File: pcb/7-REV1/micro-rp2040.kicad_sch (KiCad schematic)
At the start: 60 parts, among them J201 Conn_01x03, J202 TYPE-C-31-M-12, Q1 MMBT7002K, Q2 MMBT7002K, SW101 TS3425BA 098 2.5H 250gf, SW102 TS3315A 250gf 025, U1 RP2350B, U102 W25Q128JVSIQ, U105 MT29F1G01ABAFDWB, U16 SP3002-04JTG, U3 TLV74311PDBVR, U401 ME6211A33PG-N, U8 APS6404L-3SQR-ZR, Y101 ABM8-272-T3

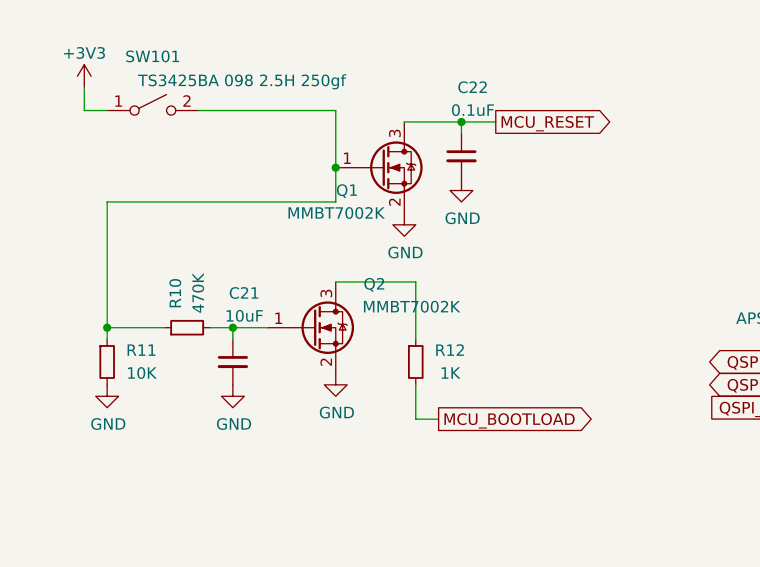
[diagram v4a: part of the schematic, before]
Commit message: replace MMBT7002K in SOT-23 with 2N7002T in SOT-523
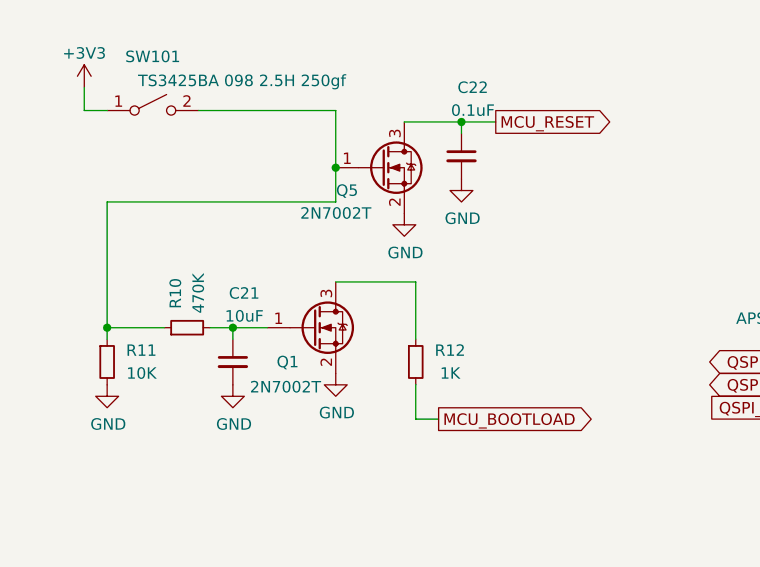
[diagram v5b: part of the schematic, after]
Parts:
- removed Q2: MMBT7002K, Package_TO_SOT_SMD:SOT-23, symbol Transistor_FET:BSS138
- added Q5: 2N7002T, Package_TO_SOT_SMD:SOT-523, symbol Transistor_FET:BSS138
- Q1: value MMBT7002K -> 2N7002T; footprint Package_TO_SOT_SMD:SOT-23 -> Package_TO_SOT_SMD:SOT-523
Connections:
- net GND: now also Q5.2 (S)
- net MCU_RESET: now also Q5.3 (D); no longer Q1.3 (D)
- net at R10.1, R11.1, SW101.2 (B): now also Q5.1 (G); no longer Q1.1 (G)
- net at C21.1, R10.2: now also Q1.1 (G)
- net at R12.1: now also Q1.3 (D)
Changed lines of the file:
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@@
 	)
 	(junction
-		(at 54.61 127)
-		(diameter 0)
-		(color 0 0 0 0)
-	)
-	(junction
 		(at 114.3 36.83)
 		(diameter 0)
@@
 		(color 0 0 0 0)
 	)
+	(junction
+		(at 54.61 127)
+		(diameter 0)
+		(color 0 0 0 0)
+	)
 	(no_connect
 		(at 90.17 41.91)
@@
 	(wire
 		(pts
-			(xy 54.61 130.81) (xy 54.61 127)
-		)
-		(stroke
-			(width 0)
-			(type default)
-		)
-	)
-	(wire
-		(pts
 			(xy 228.6 146.05) (xy 219.71 146.05)
 		)
@@
 	(wire
 		(pts
+			(xy 54.61 127) (xy 54.61 130.81)
+		)
+		(stroke
+			(width 0)
+			(type default)
+		)
+	)
+	(wire
+		(pts
 			(xy 325.12 41.91) (xy 327.66 41.91)
 		)
@@
 	)
 	(symbol
-		(lib_id "Transistor_FET:BSS138")
-		(at 52.07 144.78 0)
-		(unit 1)
-		(exclude_from_sim no)
-		(in_bom yes)
-		(on_board yes)
-		(dnp no)
-		(property "Reference" "Q2"
-			(at 58.928 139.954 0)
-			(effects
-				(font
-					(size 1.27 1.27)
-				)
-			)
-		)
-		(property "Value" "MMBT7002K"
-			(at 62.992 142.494 0)
-			(effects
-				(font
-					(size 1.27 1.27)
-				)
-			)
-		)
-		(property "Footprint" "Package_TO_SOT_SMD:SOT-23"
-			(at 57.15 146.685 0)
-			(effects
-				(font
-					(size 1.27 1.27)
-					(italic yes)
-				)
-				(justify left)
-				(hide yes)
-			)
-		)
-		(property "Datasheet" "https://www.fairchildsemi.com/datasheets/BS/BSS138.pdf"
-			(at 52.07 144.78 0)
-			(effects
-				(font
-					(size 1.27 1.27)
-				)
-				(justify left)
-				(hide yes)
-			)
-		)
-		(property "Description" ""
-			(at 52.07 144.78 0)
-			(effects
-				(font
-					(size 1.27 1.27)
-				)
-				(hide yes)
-			)
-		)
-		(property "RMB" "0.140017"
-			(at 52.07 144.78 0)
-			(effects
-				(font
-					(size 1.27 1.27)
-				)
-				(hide yes)
-			)
-		)
-		(property "Supplier" "https://item.szlcsc.com/544697.html"
-			(at 52.07 144.78 0)
-			(effects
-				(font
-					(size 1.27 1.27)
-				)
-				(hide yes)
-			)
-		)
-		(pin "1"
-		)
-		(pin "2"
-		)
-		(pin "3"
-		)
-		(instances
-			(project "7-REV0"
-				(path "/1f56410a-eaac-4444-b0f7-cfd3531e22ac/00000000-0000-0000-0000-000060c8ec36"
-					(reference "Q2")
-					(unit 1)
-				)
-			)
-		)
-	)
-	(symbol
 		(lib_id "power:GND")
 		(at 120.65 163.83 0)
@@
 	)
 	(symbol
+		(lib_id "Transistor_FET:BSS138")
+		(at 59.69 127 0)
+		(unit 1)
+		(exclude_from_sim no)
+		(in_bom yes)
+		(on_board yes)
+		(dnp no)
+		(property "Reference" "Q5"
+			(at 55.88 129.54 0)
+			(effects
+				(font
+					(size 1.27 1.27)
+				)
+			)
+		)
+		(property "Value" "2N7002T"
+			(at 54.61 132.08 0)
+			(effects
+				(font
+					(size 1.27 1.27)
+				)
+			)
+		)
+		(property "Footprint" "Package_TO_SOT_SMD:SOT-523"
+			(at 64.77 128.905 0)
+			(effects
+				(font
+					(size 1.27 1.27)
+					(italic yes)
+				)
+				(justify left)
+				(hide yes)
+			)
+		)
+		(property "Datasheet" "https://www.onsemi.com/download/data-sheet/pdf/2n7002t-d.pdf"
+			(at 59.69 127 0)
+			(effects
+				(font
+					(size 1.27 1.27)
+				)
+				(justify left)
+				(hide yes)
+			)
+		)
+		(property "Description" ""
+			(at 59.69 127 0)
+			(effects
+				(font
+					(size 1.27 1.27)
+				)
+				(hide yes)
+			)
+		)
+		(property "RMB" "0.140017"
+			(at 59.69 127 0)
+			(effects
+				(font
+					(size 1.27 1.27)
+				)
+				(hide yes)
+			)
+		)
+		(property "Supplier" "https://item.szlcsc.com/544697.html"
+			(at 59.69 127 0)
+			(effects
+				(font
+					(size 1.27 1.27)
+				)
+				(hide yes)
+			)
+		)
+		(pin "1"
+		)
+		(pin "2"
+		)
+		(pin "3"
+		)
+		(instances
+			(project "7-REV1"
+				(path "/1f56410a-eaac-4444-b0f7-cfd3531e22ac/00000000-0000-0000-0000-000060c8ec36"
+					(reference "Q5")
+					(unit 1)
+				)
+			)
+		)
+	)
+	(symbol
 		(lib_id "dp-memory:xm25qh128a")
 		(at 120.65 158.75 0)
@@
 	)
 	(symbol
-		(lib_id "Transistor_FET:BSS138")
-		(at 59.69 127 0)
-		(unit 1)
-		(exclude_from_sim no)
-		(in_bom yes)
-		(on_board yes)
-		(dnp no)
-		(property "Reference" "Q1"
-			(at 55.88 129.54 0)
-			(effects
-				(font
-					(size 1.27 1.27)
-				)
-			)
-		)
-		(property "Value" "MMBT7002K"
-			(at 54.61 132.08 0)
-			(effects
-				(font
-					(size 1.27 1.27)
-				)
-			)
-		)
-		(property "Footprint" "Package_TO_SOT_SMD:SOT-23"
-			(at 64.77 128.905 0)
-			(effects
-				(font
-					(size 1.27 1.27)
-					(italic yes)
-				)
-				(justify left)
-				(hide yes)
-			)
-		)
-		(property "Datasheet" "https://www.fairchildsemi.com/datasheets/BS/BSS138.pdf"
-			(at 59.69 127 0)
-			(effects
-				(font
-					(size 1.27 1.27)
-				)
-				(justify left)
-				(hide yes)
-			)
-		)
-		(property "Description" ""
-			(at 59.69 127 0)
-			(effects
-				(font
-					(size 1.27 1.27)
-				)
-				(hide yes)
-			)
-		)
-		(property "RMB" "0.140017"
-			(at 59.69 127 0)
-			(effects
-				(font
-					(size 1.27 1.27)
-				)
-				(hide yes)
-			)
-		)
-		(property "Supplier" "https://item.szlcsc.com/544697.html"
-			(at 59.69 127 0)
-			(effects
-				(font
-					(size 1.27 1.27)
-				)
-				(hide yes)
-			)
-		)
-		(pin "1"
-		)
-		(pin "2"
-		)
-		(pin "3"
-		)
-		(instances
-			(project "7-REV0"
-				(path "/1f56410a-eaac-4444-b0f7-cfd3531e22ac/00000000-0000-0000-0000-000060c8ec36"
-					(reference "Q1")
-					(unit 1)
-				)
-			)
-		)
-	)
-	(symbol
 		(lib_id "power:GND")
 		(at 43.18 151.13 0)
@@
 					(unit 1)
 				)
+			)
+		)
+	)
+	(symbol
+		(lib_id "Transistor_FET:BSS138")
+		(at 52.07 144.78 0)
+		(unit 1)
+		(exclude_from_sim no)
+		(in_bom yes)
+		(on_board yes)
+		(dnp no)
+		(property "Reference" "Q1"
+			(at 49.276 148.59 0)
+			(effects
+				(font
+					(size 1.27 1.27)
+				)
+			)
+		)
+		(property "Value" "2N7002T"
+			(at 49.022 151.384 0)
+			(effects
+				(font
+					(size 1.27 1.27)
+				)
+			)
+		)
+		(property "Footprint" "Package_TO_SOT_SMD:SOT-523"
+			(at 57.15 146.685 0)
+			(effects
+				(font
+					(size 1.27 1.27)
+					(italic yes)
+				)
+				(justify left)
+				(hide yes)
+			)
+		)
+		(property "Datasheet" "https://www.onsemi.com/download/data-sheet/pdf/2n7002t-d.pdf"
+			(at 52.07 144.78 0)
+			(effects
+				(font
+					(size 1.27 1.27)
+				)
+				(justify left)
+				(hide yes)
+			)
+		)
+		(property "Description" ""
+			(at 52.07 144.78 0)
+			(effects
+				(font
+					(size 1.27 1.27)
+				)
+				(hide yes)
+			)
+		)
+		(property "RMB" "0.140017"
+			(at 52.07 144.78 0)
+			(effects
+				(font
+					(size 1.27 1.27)
+				)
+				(hide yes)
+			)
+		)
+		(property "Supplier" "https://item.szlcsc.com/544697.html"
+			(at 52.07 144.78 0)
+			(effects
+				(font
+					(size 1.27 1.27)
+				)
+				(hide yes)
+			)
+		)
+		(pin "1"
+		)
+		(pin "2"
+		)
+		(pin "3"
+		)
+		(instances
+			(project "7-REV1"
+				(path "/1f56410a-eaac-4444-b0f7-cfd3531e22ac/00000000-0000-0000-0000-000060c8ec36"
+					(reference "Q1")
+					(unit 1)
+				)

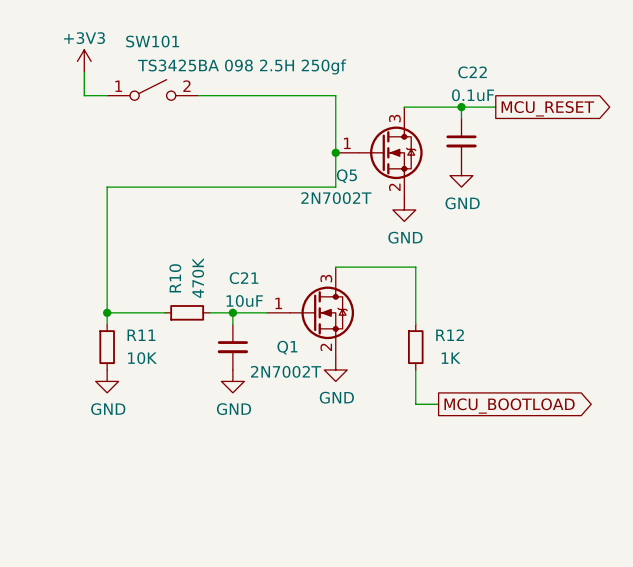
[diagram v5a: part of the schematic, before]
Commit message: replace 10µF / 0402 cap with 4.7µF / 0402 to save one BOM line
- new reset / bootloader circuit
- adjust resistor to 560k
- exact values have to be tested (cap varies by mfg due to voltage derating)
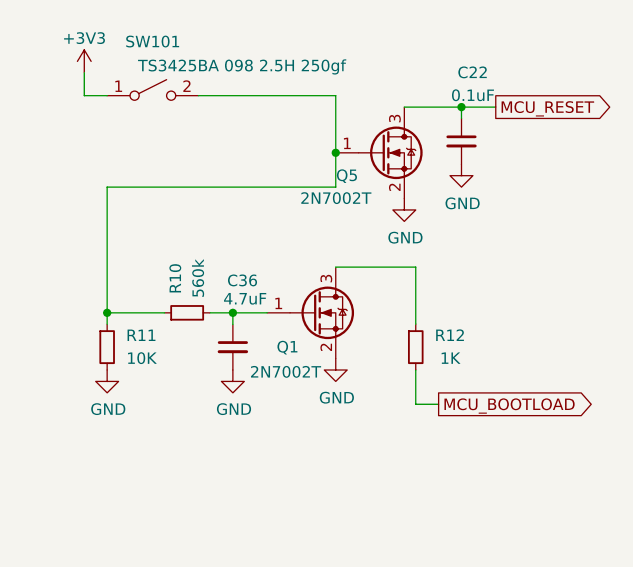
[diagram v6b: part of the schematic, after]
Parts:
- removed C21: 10uF, Capacitor_SMD:C_0402_1005Metric, symbol Device:C_Small
- added C36: 4.7uF, Capacitor_SMD:C_0402_1005Metric, symbol Device:C_Small
- R10: value 470K -> 560k
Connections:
- net GND: now also C36.2
- net at Q1.1 (G), R10.2: now also C36.1
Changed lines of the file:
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@@
+	)
+	(symbol
+		(lib_id "power:GND")
+		(at 54.61 149.86 0)
+		(unit 1)
+		(exclude_from_sim no)
+		(in_bom yes)
+		(on_board yes)
+		(dnp no)
+		(property "Reference" "#PWR072"
+			(at 54.61 156.21 0)
+			(effects
+				(font
+					(size 1.27 1.27)
+				)
+				(hide yes)
+			)
+		)
+		(property "Value" "GND"
+			(at 54.737 154.2542 0)
+			(effects
+				(font
+					(size 1.27 1.27)
+				)
+			)
+		)
+		(property "Footprint" ""
+			(at 54.61 149.86 0)
+			(effects
+				(font
+					(size 1.27 1.27)
+				)
+				(hide yes)
+			)
+		)
+		(property "Datasheet" ""
+			(at 54.61 149.86 0)
+			(effects
+				(font
+					(size 1.27 1.27)
+				)
+				(hide yes)
+			)
+		)
+		(property "Description" ""
+			(at 54.61 149.86 0)
+			(effects
+				(font
+					(size 1.27 1.27)
+				)
+				(hide yes)
+			)
+		)
+		(pin "1"
+		)
+		(instances
+			(project "7-REV0"
+				(path "/1f56410a-eaac-4444-b0f7-cfd3531e22ac/00000000-0000-0000-0000-000060c8ec36"
+					(reference "#PWR072")
+					(unit 1)
+				)
+			)
+		)
+	)
+	(symbol
+		(lib_id "Device:C_Small")
+		(at 368.3 40.64 0)
+		(unit 1)
+		(exclude_from_sim no)
+		(in_bom yes)
+		(on_board yes)
+		(dnp no)
+		(property "Reference" "C10"
+			(at 365.76 39.37 0)
+			(effects
+				(font
+					(size 1.27 1.27)
+				)
+				(justify right)
+			)
+		)
+		(property "Value" "4.7uF"
+			(at 365.76 41.91 0)
+			(effects
+				(font
+					(size 1.27 1.27)
+				)
+				(justify right)
+			)
+		)
+		(property "Footprint" "Capacitor_SMD:C_0402_1005Metric"
+			(at 368.3 40.64 0)
+			(effects
+				(font
+					(size 1.27 1.27)
+				)
+				(hide yes)
+			)
+		)
+		(property "Datasheet" "~"
+			(at 368.3 40.64 0)
+			(effects
+				(font
+					(size 1.27 1.27)
+				)
+				(hide yes)
+			)
+		)
+		(property "Description" ""
+			(at 368.3 40.64 0)
+			(effects
+				(font
+					(size 1.27 1.27)
+				)
+				(hide yes)
+			)
+		)
+		(property "RMB" "0.037726"
+			(at 368.3 40.64 0)
+			(effects
+				(font
+					(size 1.27 1.27)
+				)
+				(hide yes)
+			)
+		)
+		(property "Supplier" "https://item.szlcsc.com/1877.html"
+			(at 368.3 40.64 0)
+			(effects
+				(font
+					(size 1.27 1.27)
+				)
+				(hide yes)
+			)
+		)
+		(pin "1"
+		)
+		(pin "2"
+		)
+		(instances
+			(project "bp6-rev2"
+				(path "/1f56410a-eaac-4444-b0f7-cfd3531e22ac/00000000-0000-0000-0000-000060c8ec36"
+					(reference "C10")
+					(unit 1)
+				)
+			)
+		)
 	)
 	(symbol
@@
 		(on_board yes)
 		(dnp no)
-		(property "Reference" "C21"
-			(at 44.45 140.97 0)
-			(effects
-				(font
-					(size 1.27 1.27)
-				)
-			)
-		)
-		(property "Value" "10uF"
-			(at 44.45 143.51 0)
-			(effects
-				(font
-					(size 1.27 1.27)
-				)
+		(property "Reference" "C36"
+			(at 45.974 141.224 0)
+			(effects
+				(font
+					(size 1.27 1.27)
+				)
+				(justify right)
+			)
+		)
+		(property "Value" "4.7uF"
+			(at 46.99 143.256 0)
+			(effects
+				(font
+					(size 1.27 1.27)
+				)
+				(justify right)
 			)
 		)
@@
 			)
 		)
-		(property "RMB" "0.043101"
+		(property "RMB" "0.037726"
 			(at 43.18 148.59 0)
 			(effects
@@
 			)
 		)
-		(property "Supplier" "https://item.szlcsc.com/108589.html"
+		(property "Supplier" "https://item.szlcsc.com/1877.html"
 			(at 43.18 148.59 0)
 			(effects
@@
 		)
 		(instances
-			(project "7-REV0"
-				(path "/1f56410a-eaac-4444-b0f7-cfd3531e22ac/00000000-0000-0000-0000-000060c8ec36"
-					(reference "C21")
-					(unit 1)
-				)
-			)
-		)
-	)
-	(symbol
-		(lib_id "power:GND")
-		(at 54.61 149.86 0)
-		(unit 1)
-		(exclude_from_sim no)
-		(in_bom yes)
-		(on_board yes)
-		(dnp no)
-		(property "Reference" "#PWR072"
-			(at 54.61 156.21 0)
-			(effects
-				(font
-					(size 1.27 1.27)
-				)
-				(hide yes)
-			)
-		)
-		(property "Value" "GND"
-			(at 54.737 154.2542 0)
-			(effects
-				(font
-					(size 1.27 1.27)
-				)
-			)
-		)
-		(property "Footprint" ""
-			(at 54.61 149.86 0)
-			(effects
-				(font
-					(size 1.27 1.27)
-				)
-				(hide yes)
-			)
-		)
-		(property "Datasheet" ""
-			(at 54.61 149.86 0)
-			(effects
-				(font
-					(size 1.27 1.27)
-				)
-				(hide yes)
-			)
-		)
-		(property "Description" ""
-			(at 54.61 149.86 0)
-			(effects
-				(font
-					(size 1.27 1.27)
-				)
-				(hide yes)
-			)
-		)
-		(pin "1"
-		)
-		(instances
-			(project "7-REV0"
-				(path "/1f56410a-eaac-4444-b0f7-cfd3531e22ac/00000000-0000-0000-0000-000060c8ec36"
-					(reference "#PWR072")
-					(unit 1)
-				)
-			)
-		)
-	)
-	(symbol
-		(lib_id "Device:C_Small")
-		(at 368.3 40.64 0)
-		(unit 1)
-		(exclude_from_sim no)
-		(in_bom yes)
-		(on_board yes)
-		(dnp no)
-		(property "Reference" "C10"
-			(at 365.76 39.37 0)
-			(effects
-				(font
-					(size 1.27 1.27)
-				)
-				(justify right)
-			)
-		)
-		(property "Value" "4.7uF"
-			(at 365.76 41.91 0)
-			(effects
-				(font
-					(size 1.27 1.27)
-				)
-				(justify right)
-			)
-		)
-		(property "Footprint" "Capacitor_SMD:C_0402_1005Metric"
-			(at 368.3 40.64 0)
-			(effects
-				(font
-					(size 1.27 1.27)
-				)
-				(hide yes)
-			)
-		)
-		(property "Datasheet" "~"
-			(at 368.3 40.64 0)
-			(effects
-				(font
-					(size 1.27 1.27)
-				)
-				(hide yes)
-			)
-		)
-		(property "Description" ""
-			(at 368.3 40.64 0)
-			(effects
-				(font
-					(size 1.27 1.27)
-				)
-				(hide yes)
-			)
-		)
-		(property "RMB" "0.037726"
-			(at 368.3 40.64 0)
-			(effects
-				(font
-					(size 1.27 1.27)
-				)
-				(hide yes)
-			)
-		)
-		(property "Supplier" "https://item.szlcsc.com/1877.html"
-			(at 368.3 40.64 0)
-			(effects
-				(font
-					(size 1.27 1.27)
-				)
-				(hide yes)
-			)
-		)
-		(pin "1"
-		)
-		(pin "2"
-		)
-		(instances
-			(project "bp6-rev2"
-				(path "/1f56410a-eaac-4444-b0f7-cfd3531e22ac/00000000-0000-0000-0000-000060c8ec36"
-					(reference "C10")
+			(project "7-REV1"
+				(path "/1f56410a-eaac-4444-b0f7-cfd3531e22ac/00000000-0000-0000-0000-000060c8ec36"
+					(reference "C36")
 					(unit 1)
 				)
@@
 			)
 		)
-		(property "Value" "470K"
+		(property "Value" "560k"
 			(at 39.37 140.97 0)
 			(effects
